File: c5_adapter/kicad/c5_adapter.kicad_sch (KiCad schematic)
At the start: 10 parts, among them J1 Conn_01x10, J2 Conn_01x10, J3 Conn_01x16, J4 Conn_01x16, J5 Conn_01x16, J6 Conn_01x16, SW2 MK-12C02-G020, U1 ESP32-C5-DevKitC-1

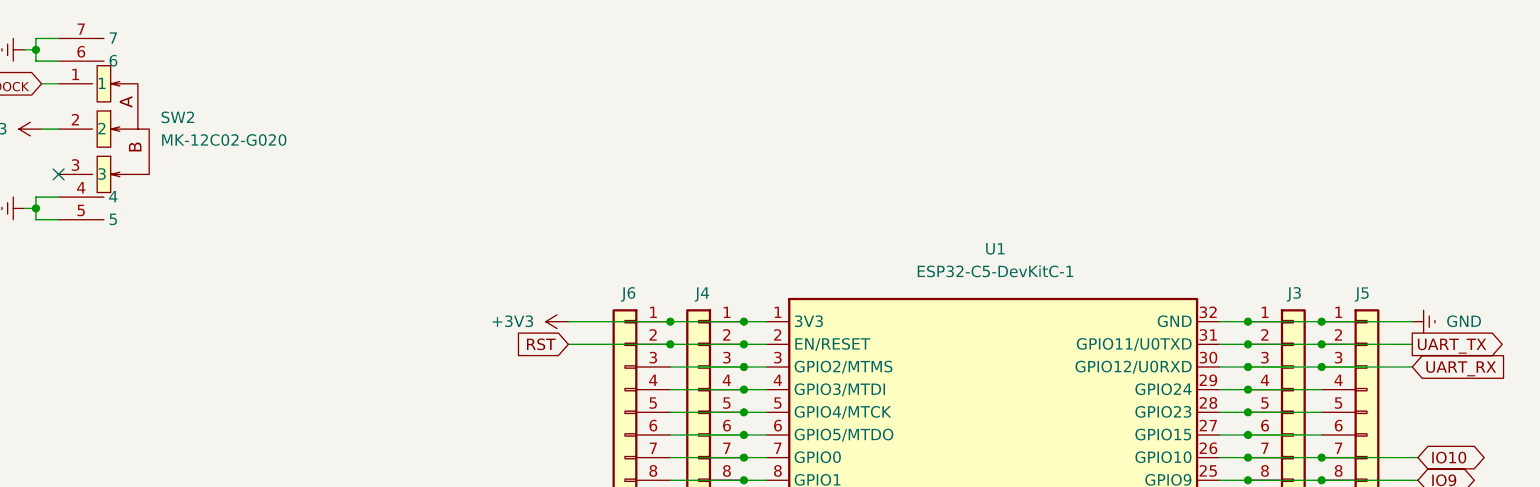
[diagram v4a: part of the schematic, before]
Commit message: Updated silkscreen on C5 adapter
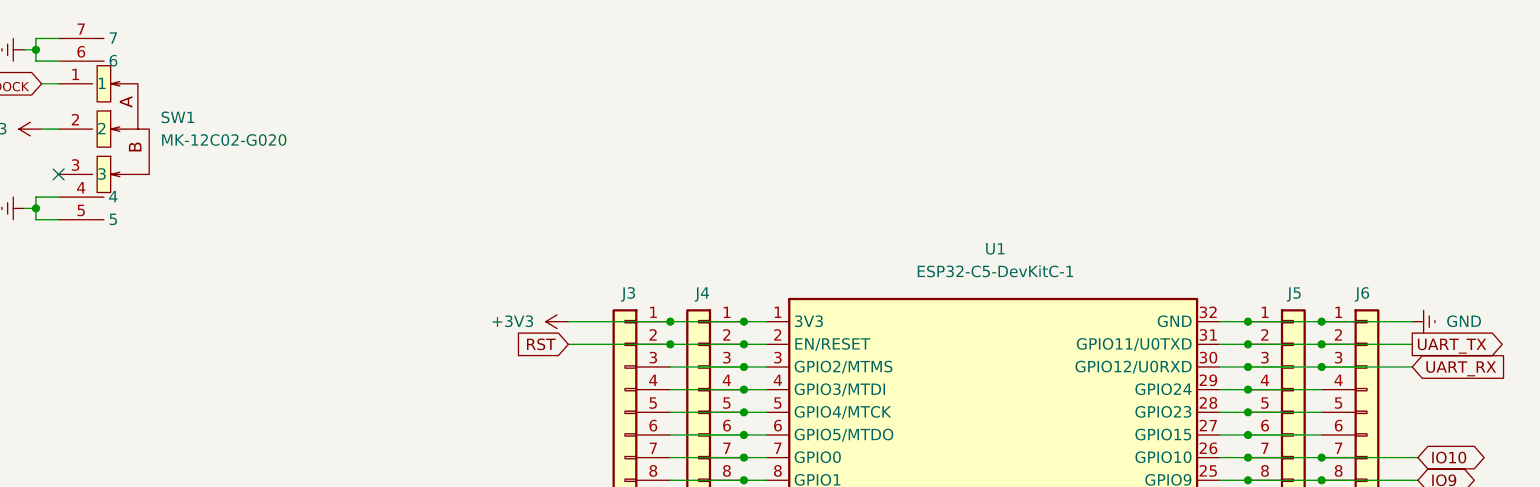
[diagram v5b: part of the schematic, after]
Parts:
- renumbered J6 to J3, J3 to J5, J5 to J6, SW2 to SW1
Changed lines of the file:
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@@
 		(dnp no)
 		(fields_autoplaced yes)
-		(property "Reference" "#PWR011"
+		(property "Reference" "#PWR05"
 			(at 82.55 60.325 0)
 			(hide yes)
@@
 			(project "c5_adapter"
 				(path "/4ea9e048-096c-4569-98b9-ff311a85c85d"
-					(reference "#PWR011")
+					(reference "#PWR05")
 					(unit 1)
 				)
@@
 		(dnp no)
 		(fields_autoplaced yes)
-		(property "Reference" "#PWR02"
+		(property "Reference" "#PWR03"
 			(at 82.55 175.895 0)
 			(hide yes)
@@
 			(project "c5_adapter"
 				(path "/4ea9e048-096c-4569-98b9-ff311a85c85d"
-					(reference "#PWR02")
+					(reference "#PWR03")
 					(unit 1)
 				)
@@
 		(dnp no)
 		(fields_autoplaced yes)
-		(property "Reference" "#PWR04"
+		(property "Reference" "#PWR08"
 			(at 154.305 106.045 0)
 			(hide yes)
@@
 			(project "c5_adapter"
 				(path "/4ea9e048-096c-4569-98b9-ff311a85c85d"
-					(reference "#PWR04")
+					(reference "#PWR08")
 					(unit 1)
 				)
@@
 		(in_pos_files yes)
 		(dnp no)
-		(property "Reference" "J3"
+		(property "Reference" "J5"
 			(at 230.505 69.85 0)
 			(show_name no)
@@
 			(project "c5_adapter"
 				(path "/4ea9e048-096c-4569-98b9-ff311a85c85d"
-					(reference "J3")
+					(reference "J5")
 					(unit 1)
 				)
@@
 		(dnp no)
 		(fields_autoplaced yes)
-		(property "Reference" "#PWR06"
+		(property "Reference" "#PWR010"
 			(at 250.825 73.025 0)
 			(hide yes)
@@
 			(project "c5_adapter"
 				(path "/4ea9e048-096c-4569-98b9-ff311a85c85d"
-					(reference "#PWR06")
+					(reference "#PWR010")
 					(unit 1)
 				)
@@
 		(in_pos_files yes)
 		(dnp no)
-		(property "Reference" "J6"
+		(property "Reference" "J3"
 			(at 157.48 69.85 0)
 			(show_name no)
@@
 			(project "c5_adapter"
 				(path "/4ea9e048-096c-4569-98b9-ff311a85c85d"
-					(reference "J6")
+					(reference "J3")
 					(unit 1)
 				)
@@
 		(dnp no)
 		(fields_autoplaced yes)
-		(property "Reference" "#PWR03"
+		(property "Reference" "#PWR07"
 			(at 153.67 73.025 0)
 			(hide yes)
@@
 			(project "c5_adapter"
 				(path "/4ea9e048-096c-4569-98b9-ff311a85c85d"
-					(reference "#PWR03")
+					(reference "#PWR07")
 					(unit 1)
 				)
@@
 		(dnp no)
 		(fields_autoplaced yes)
-		(property "Reference" "#PWR010"
+		(property "Reference" "#PWR06"
 			(at 94.615 51.435 0)
 			(hide yes)
@@
 			(project "c5_adapter"
 				(path "/4ea9e048-096c-4569-98b9-ff311a85c85d"
-					(reference "#PWR010")
+					(reference "#PWR06")
 					(unit 1)
 				)
@@
 		(dnp no)
 		(fields_autoplaced yes)
-		(property "Reference" "#PWR08"
+		(property "Reference" "#PWR012"
 			(at 250.825 108.585 0)
 			(hide yes)
@@
 			(project "c5_adapter"
 				(path "/4ea9e048-096c-4569-98b9-ff311a85c85d"
-					(reference "#PWR08")
+					(reference "#PWR012")
 					(unit 1)
 				)
@@
 		(dnp no)
 		(fields_autoplaced yes)
-		(property "Reference" "SW2"
+		(property "Reference" "SW1"
 			(at 104.14 50.1649 90)
 			(show_name no)
@@
 			(project "c5_adapter"
 				(path "/4ea9e048-096c-4569-98b9-ff311a85c85d"
-					(reference "SW2")
+					(reference "SW1")
 					(unit 1)
 				)
@@
 		(in_pos_files yes)
 		(dnp no)
-		(property "Reference" "J5"
+		(property "Reference" "J6"
 			(at 238.125 69.85 0)
 			(show_name no)
@@
 			(project "c5_adapter"
 				(path "/4ea9e048-096c-4569-98b9-ff311a85c85d"
-					(reference "J5")
+					(reference "J6")
 					(unit 1)
 				)
@@
 		(dnp no)
 		(fields_autoplaced yes)
-		(property "Reference" "#PWR013"
+		(property "Reference" "#PWR04"
 			(at 82.55 42.545 0)
 			(hide yes)
@@
 			(project "c5_adapter"
 				(path "/4ea9e048-096c-4569-98b9-ff311a85c85d"
-					(reference "#PWR013")
+					(reference "#PWR04")
 					(unit 1)
 				)
@@
 		(dnp no)
 		(fields_autoplaced yes)
-		(property "Reference" "#PWR09"
+		(property "Reference" "#PWR02"
 			(at 79.375 107.315 0)
 			(hide yes)
@@
 			(project "c5_adapter"
 				(path "/4ea9e048-096c-4569-98b9-ff311a85c85d"
-					(reference "#PWR09")
+					(reference "#PWR02")
 					(unit 1)
 				)
@@
 		(dnp no)
 		(fields_autoplaced yes)
-		(property "Reference" "#PWR05"
+		(property "Reference" "#PWR09"
 			(at 144.145 108.585 0)
 			(hide yes)
@@
 			(project "c5_adapter"
 				(path "/4ea9e048-096c-4569-98b9-ff311a85c85d"
-					(reference "#PWR05")
+					(reference "#PWR09")
 					(unit 1)
 				)
@@
 		(dnp no)
 		(fields_autoplaced yes)
-		(property "Reference" "#PWR07"
+		(property "Reference" "#PWR011"
 			(at 250.825 100.965 0)
 			(hide yes)
@@
 			(project "c5_adapter"
 				(path "/4ea9e048-096c-4569-98b9-ff311a85c85d"
-					(reference "#PWR07")
-					(unit 1)
-				)
+					(reference "#PWR011")
+					(unit 1)
+				)
